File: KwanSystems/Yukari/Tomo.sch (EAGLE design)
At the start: 21 parts, among them U1 NCP1402, U2 741034

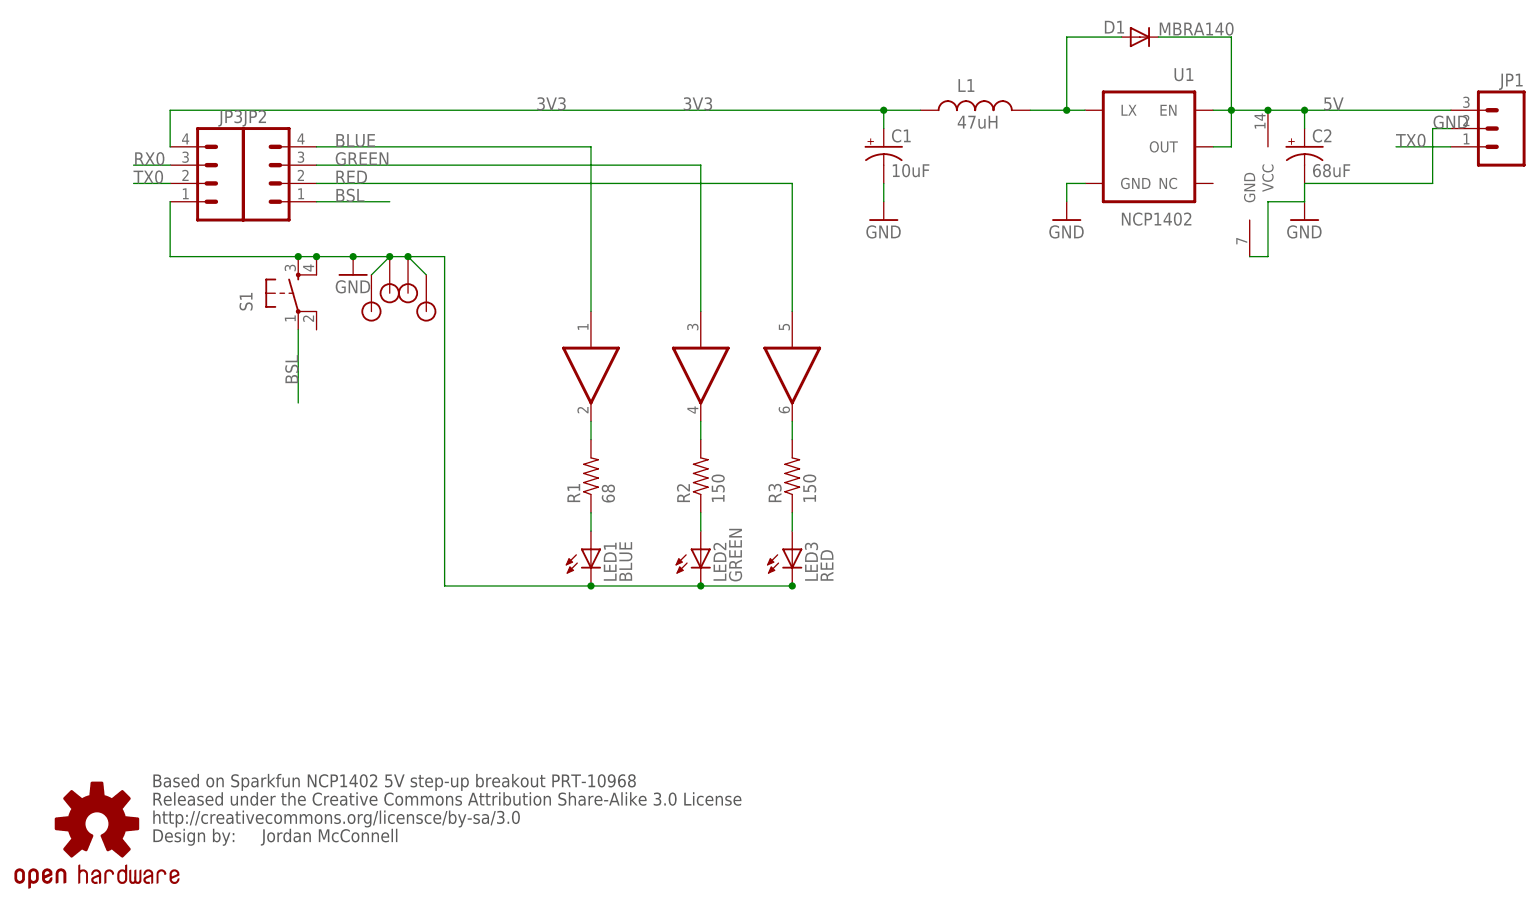
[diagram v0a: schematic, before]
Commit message: Added LegoClassicSpace.svg after checking local copy. We'll see how the pull works
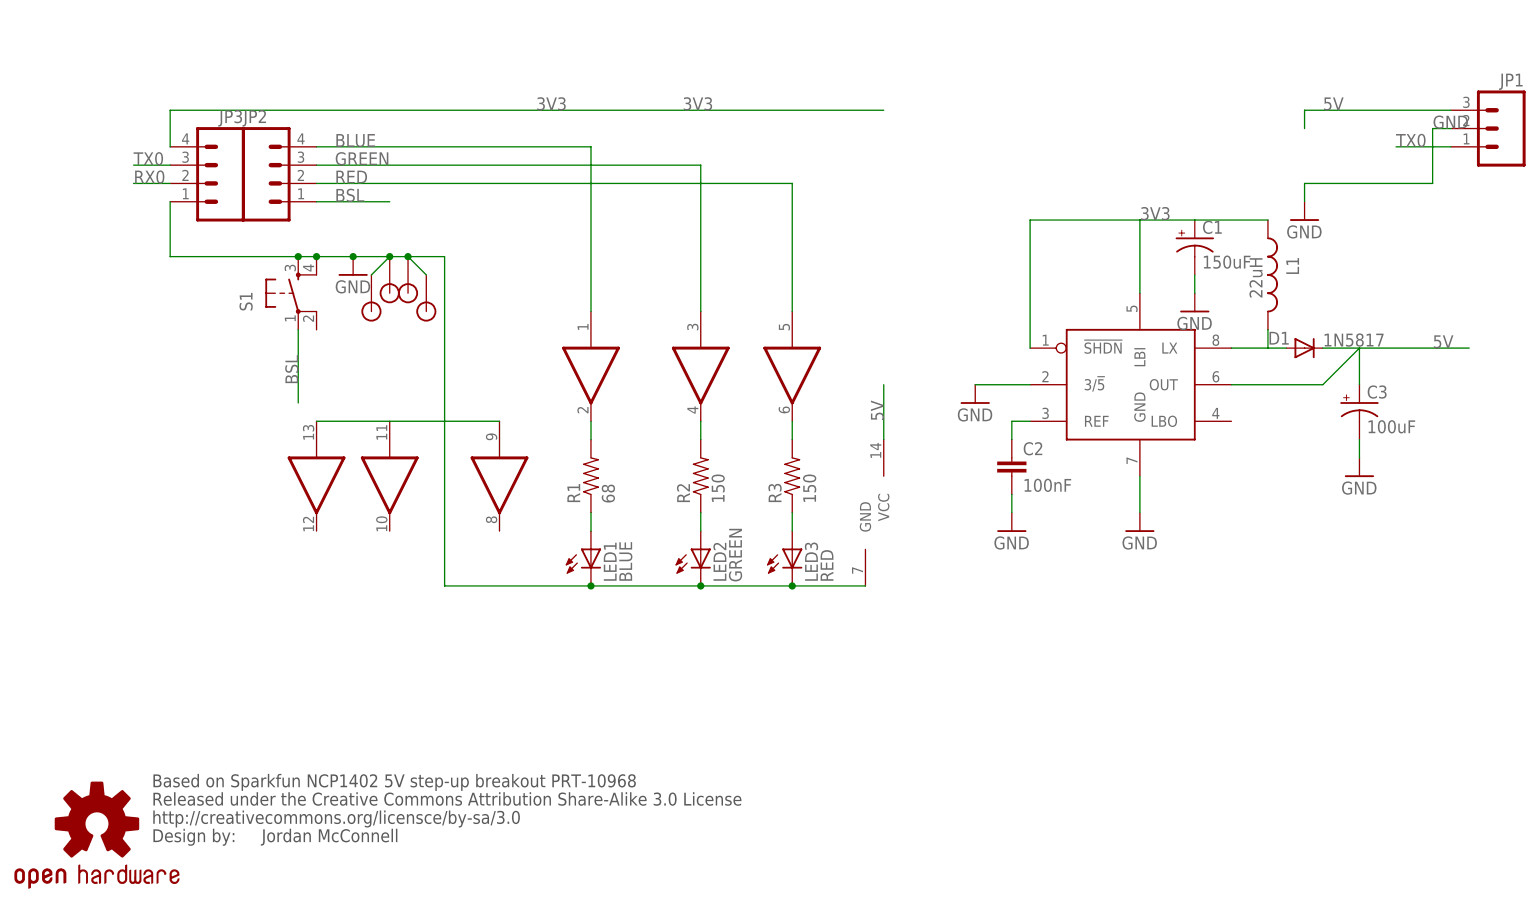
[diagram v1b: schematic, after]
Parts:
- removed U1: NCP1402, SparkFun:V_REG_NCP1400SOT23-5
- added C3: 100uF, SparkFun-Capacitors:CAP_POLPTH1
- added U$2: MAX756, KwanSystems:MAX756
- C1: value 10uF -> 150uF; device SparkFun:CAP_POL1206 -> SparkFun-Capacitors:CAP_POLPTH1; DIGIKEY (none) -> 445-1387-1-ND
- C2: value 68uF -> 100nF; device SparkFun:CAP_POL3528 -> SparkFun-Capacitors:CAPPTH
- D1: value MBRA140 -> 1N5817; device SparkFun:DIODESMA -> SparkFun-DiscreteSemi:DIODE1N4148; DIGIKEY (none) -> MBRA140T3GOSCT-ND
- JP1, JP2, JP3, U$1, U$3, U$4, U$5, U$6: DIGIKEY (none) -> $NOPART
- L1: value 47uH -> 22uH; DIGIKEY (none) -> 308-2116-ND
- LED1: DIGIKEY (none) -> 67-1751-ND
- LED2: DIGIKEY (none) -> 160-1684-ND
- LED3: DIGIKEY (none) -> 754-1277-ND
- R1: DIGIKEY (none) -> CF14JT68R0CT-ND
- R2, R3: DIGIKEY (none) -> CF14JT150RCT-ND
- U2: DIGIKEY (none) -> 296-33703-5-ND
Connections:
- new net N$8: C2.1, U$2.REF
- net 3V3: now also U$2.!SHDN, U$2.LBI
- net 5V: now also C3.+, U$2.OUT; no longer C2.+, U1.EN, U1.OUT
- net GND: now also C2.2, C3.-, U$2.3/!5, U$2.GND, U2D.IN, U2E.IN, U2F.IN; no longer C2.-, U1.GND
- net N$3: now also U$2.LX; no longer U1.LX
- net RX0: now also JP3.2; no longer JP3.3
- net TX0: now also JP3.3; no longer JP3.2
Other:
- moved on the sheet: C1, D1, L1
